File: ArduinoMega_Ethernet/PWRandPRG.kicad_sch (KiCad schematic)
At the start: 91 parts, among them J1 RJ45_Amphenol_RJMG1BD3B8K1ANR, J11 Micro_SD_Card_Det_Hirose_DM3AT, J9 PROGRAM_POWER_USBC, U2 CH340C, U3 ISM330DHCX, U4 W5500, U5 LM3281, U6 74HC244, U7 SE050C2HQ1, U8 AP22804AW5, U9 MCP7940N-xST, Y2 25Mhz, Y3 Crystal_GND23

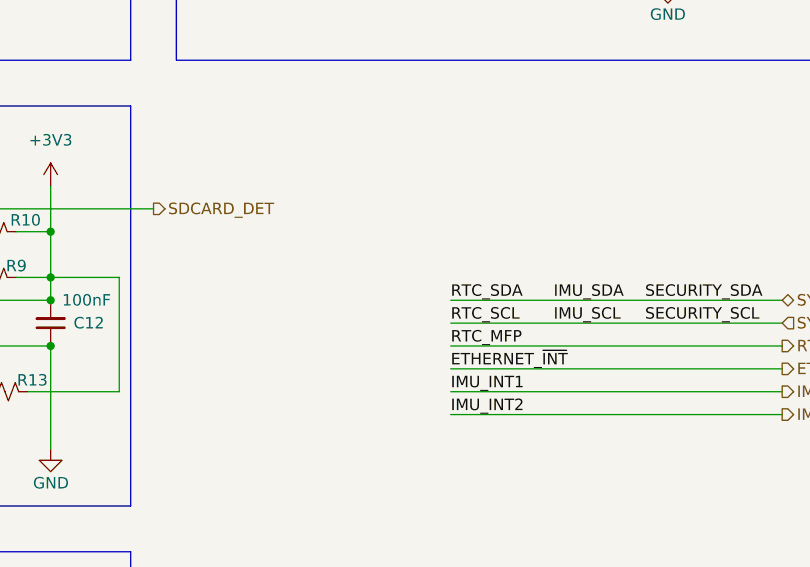
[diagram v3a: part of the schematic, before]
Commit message: I2C and Silkscreen revision
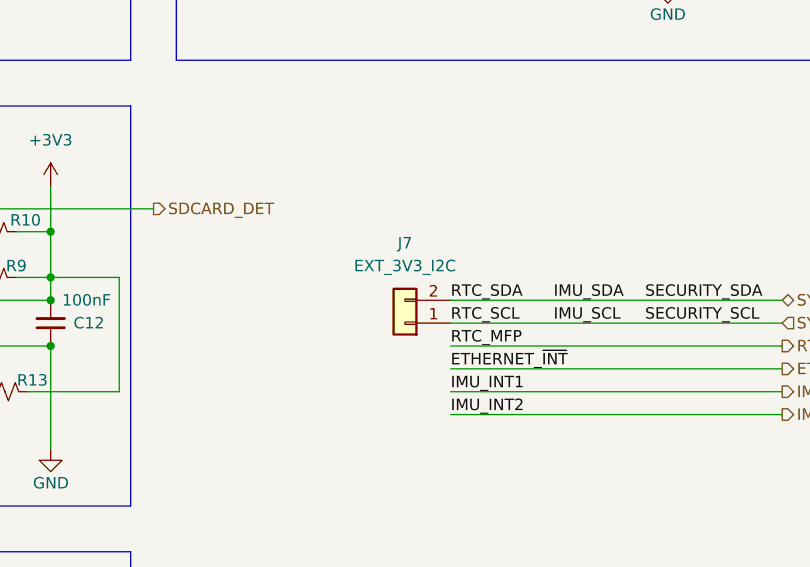
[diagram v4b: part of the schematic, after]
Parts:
- added J7: EXT_3V3_I2C, Connector_PinHeader_2.54mm:PinHeader_1x02_P2.54mm_Vertical, symbol Connector_Generic:Conn_01x02
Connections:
- net SYS_SCL: now also J7.1 (Pin_1)
- net SYS_SDA: now also J7.2 (Pin_2)
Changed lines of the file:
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@@
+	)
+	(symbol
+		(lib_id "Connector_Generic:Conn_01x02")
+		(at 240.03 208.28 180)
+		(unit 1)
+		(exclude_from_sim no)
+		(in_bom yes)
+		(on_board yes)
+		(dnp no)
+		(fields_autoplaced yes)
+		(property "Reference" "J7"
+			(at 240.03 199.39 0)
+			(effects
+				(font
+					(size 1.27 1.27)
+				)
+			)
+		)
+		(property "Value" "EXT_3V3_I2C"
+			(at 240.03 201.93 0)
+			(effects
+				(font
+					(size 1.27 1.27)
+				)
+			)
+		)
+		(property "Footprint" "Connector_PinHeader_2.54mm:PinHeader_1x02_P2.54mm_Vertical"
+			(at 240.03 208.28 0)
+			(effects
+				(font
+					(size 1.27 1.27)
+				)
+				(hide yes)
+			)
+		)
+		(property "Datasheet" "~"
+			(at 240.03 208.28 0)
+			(effects
+				(font
+					(size 1.27 1.27)
+				)
+				(hide yes)
+			)
+		)
+		(property "Description" "Generic connector, single row, 01x02, script generated (kicad-library-utils/schlib/autogen/connector/)"
+			(at 240.03 208.28 0)
+			(effects
+				(font
+					(size 1.27 1.27)
+				)
+				(hide yes)
+			)
+		)
+		(pin "1"
+		)
+		(pin "2"
+		)
+		(instances
+			(project ""
+				(path "/e63e39d7-6ac0-4ffd-8aa3-1841a4541b55/d82cdb2b-8484-4e54-a08e-6d3e852917b3"
+					(reference "J7")
+					(unit 1)
+				)
+			)
+		)
 	)
 	(symbol

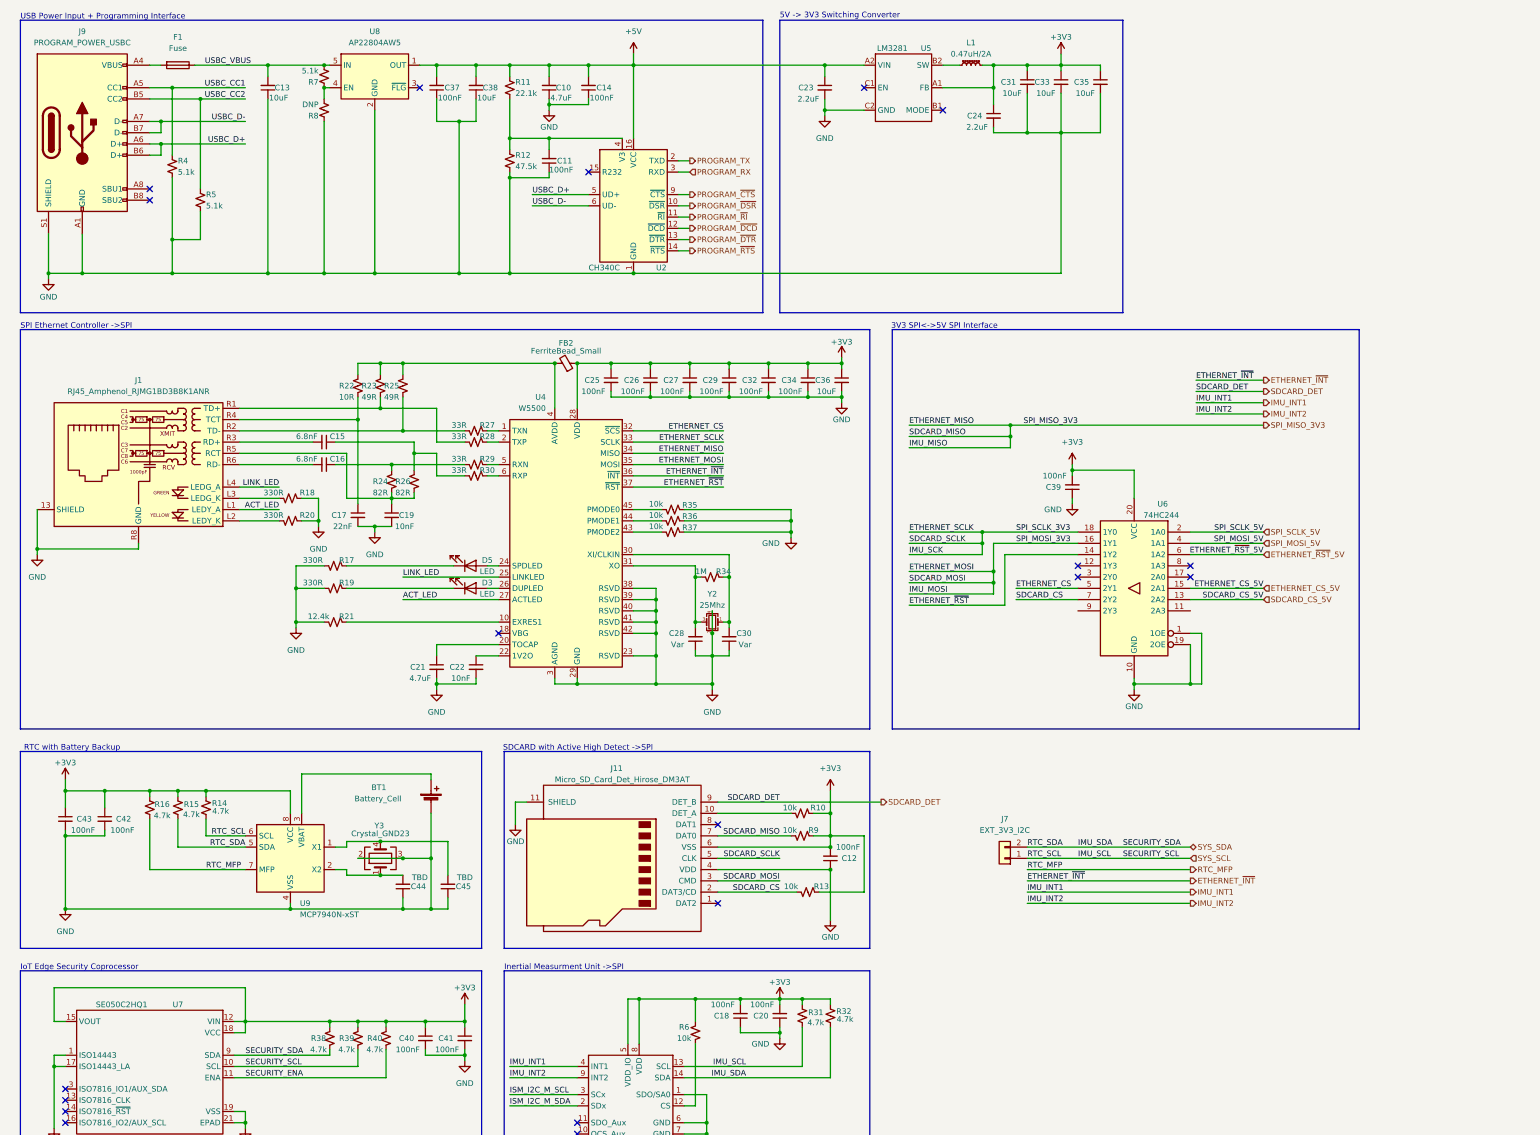
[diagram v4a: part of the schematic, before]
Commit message: update level shifter, configurable pmode
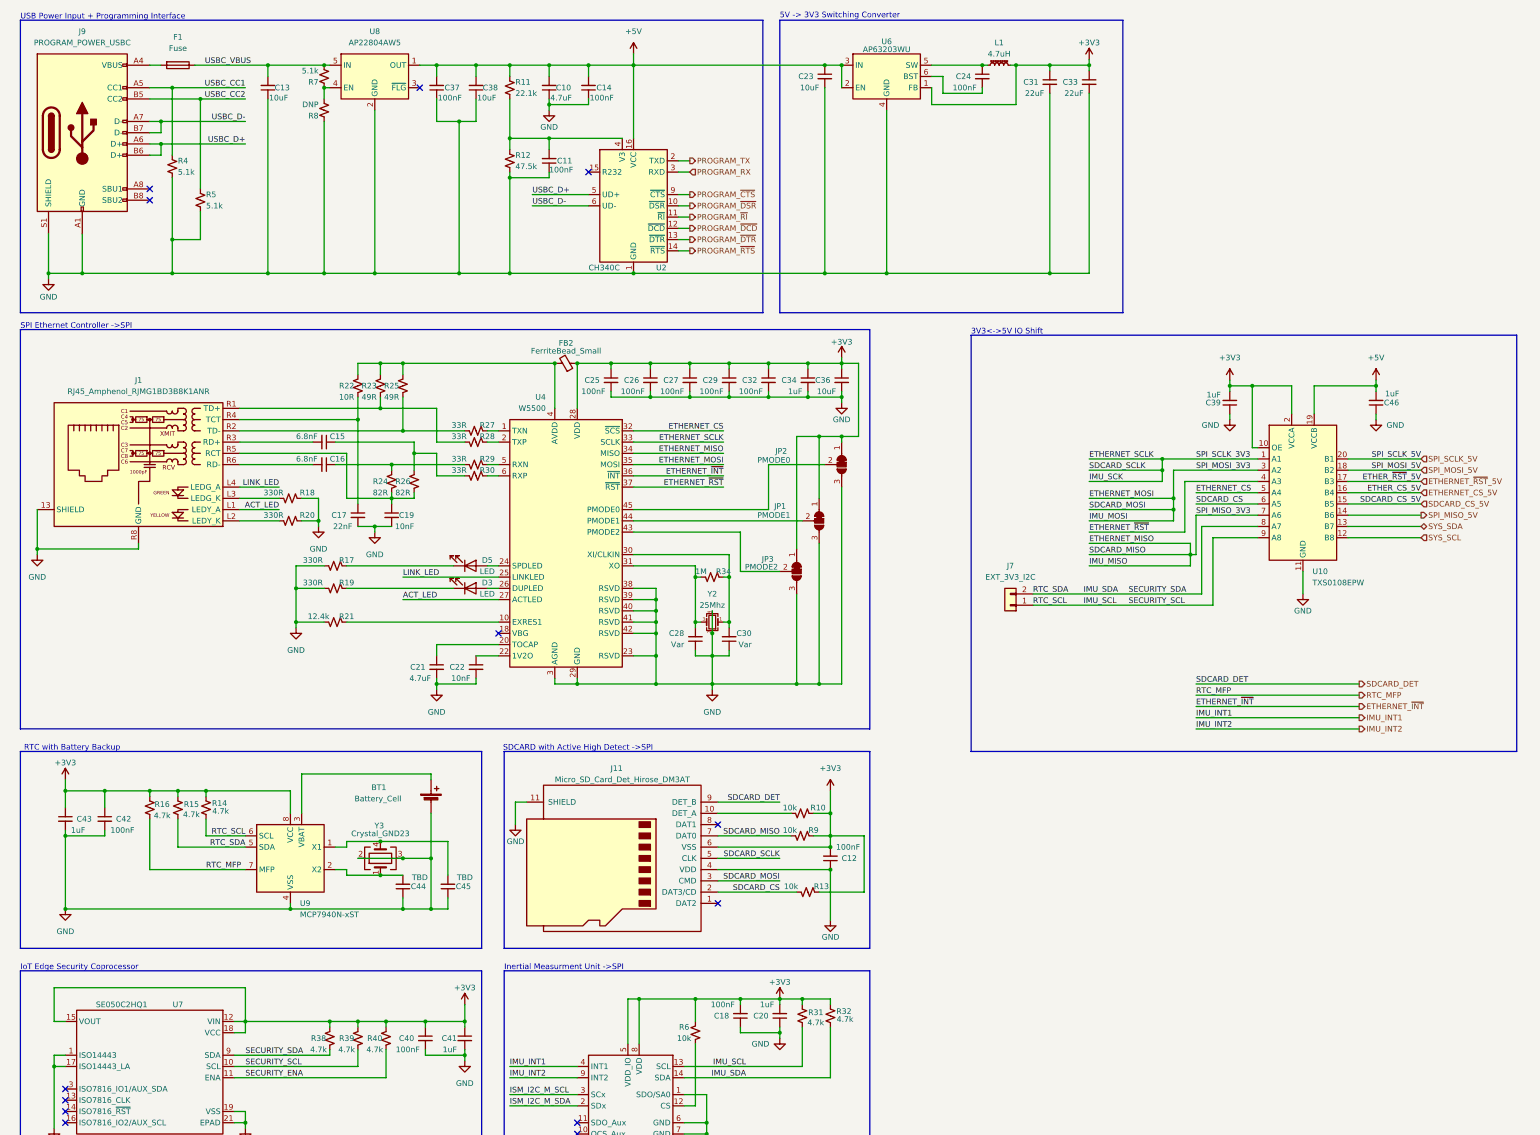
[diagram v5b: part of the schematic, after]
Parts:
- removed C35: 10uF, Capacitor_SMD:C_0805_2012Metric_Pad1.18x1.45mm_HandSolder, symbol Device:C_Small
- removed R35, R36, R37: 10k, Resistor_SMD:R_0603_1608Metric, symbol Device:R_Small_US
- removed U5: LM3281, Package_BGA:Texas_DSBGA-6_0.9x1.4mm_Layout2x3_P0.5mm, symbol DC_DC_Converters:LM3281
- removed U6: 74HC244, Package_DFN_QFN:WQFN-20-1EP_2.5x4.5mm_P0.5mm_EP1x2.9mm, symbol 74xx:74HC244
- added C46: 1uF, Capacitor_SMD:C_0603_1608Metric, symbol Device:C_Small
- added JP1: PMODE1, Jumper:SolderJumper-3_P1.3mm_Bridged12_Pad1.0x1.5mm, symbol Jumper:SolderJumper_3_Bridged12
- added JP2: PMODE0, Jumper:SolderJumper-3_P1.3mm_Bridged12_Pad1.0x1.5mm, symbol Jumper:SolderJumper_3_Bridged12
- added JP3: PMODE2, Jumper:SolderJumper-3_P1.3mm_Bridged12_Pad1.0x1.5mm, symbol Jumper:SolderJumper_3_Bridged12
- added U10: TXS0108EPW, Package_SO:TSSOP-20_4.4x6.5mm_P0.65mm, symbol Logic_LevelTranslator:TXS0108EPW
- added U6: AP63203WU, Package_TO_SOT_SMD:TSOT-23-6, symbol Regulator_Switching:AP63203WU
- C20, C34, C39, C41, C43: value 100nF -> 1uF
- C23: value 2.2uF -> 10uF
- C24: value 2.2uF -> 100nF
- C31, C33: value 10uF -> 22uF
- L1: value 0.47uH/2A -> 4.7uH; footprint Inductor_SMD:L_1206_3216Metric -> Inductor_SMD:L_1210_3225Metric_Pad1.42x2.65mm_HandSolder
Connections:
- net +3V3: now also JP1.1 (A), JP2.1 (A), JP3.1 (A), U10.10 (OE), U10.2 (VCCA), U6.1 (FB); no longer C24.1
- net +5V: now also C46.2, U10.19 (VCCB), U6.2 (EN), U6.3 (IN)
- net ETHERNET_CS: now also U10.5 (A4)
- net ETHERNET_CS_5V: now also U10.16 (B4)
- net ETHERNET_MOSI: now also U10.3 (A2)
- net ETHERNET_SCLK: now also U10.1 (A1)
- net ETHERNET_~{RST}: now also U10.4 (A3)
- net ETHERNET_~{RST}_5V: now also U10.17 (B3)
- net GND: now also C46.1, JP1.3 (B), JP2.3 (B), JP3.3 (B), U10.11 (GND), U6.4 (GND); no longer C24.2
- net SDCARD_CS: now also U10.6 (A5)
- net SDCARD_CS_5V: now also U10.15 (B5)
- net SPI_MOSI_5V: now also U10.18 (B2)
- net SPI_SCLK_5V: now also U10.20 (B1)
- net SYS_SCL: now also U10.12 (B8); no longer J7.1 (Pin_1), R14.2, R31.2, R39.2, U3.13 (SCL), U7.10 (SCL), U9.6 (SCL)
- net SYS_SDA: now also U10.13 (B7); no longer J7.2 (Pin_2), R15.2, R32.2, R38.2, U3.14 (SDA), U7.9 (SDA), U9.5 (SDA)
- net at U4.45 (PMODE0): now also JP2.2 (C)
- net at U4.44 (PMODE1): now also JP1.2 (C)
- net at L1.1: now also C24.1, U6.5 (SW)
- net at U4.43 (PMODE2): now also JP3.2 (C)
- net SPI_MISO_3V3 renamed ETHERNET_MISO
- net ETHERNET_MISO: now also U10.7 (A6)
- new net: C24.2, U6.6 (BST)
- new net IMU_SCL: J7.1 (Pin_1), R14.2, R31.2, R39.2, U10.9 (A8), U3.13 (SCL), U7.10 (SCL), U9.6 (SCL)
- new net IMU_SDA: J7.2 (Pin_2), R15.2, R32.2, R38.2, U10.8 (A7), U3.14 (SDA), U7.9 (SDA), U9.5 (SDA)
- new net SPI_MISO_5V: U10.14 (B6)
- no-connect marks 19 -> 13
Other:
- note added: "3V3<->5V IO Shift"
- note removed: "3V3 SPI<->5V SPI Interface"
- moved on the sheet: C23, C24, C31, C33, C39, J7, L1

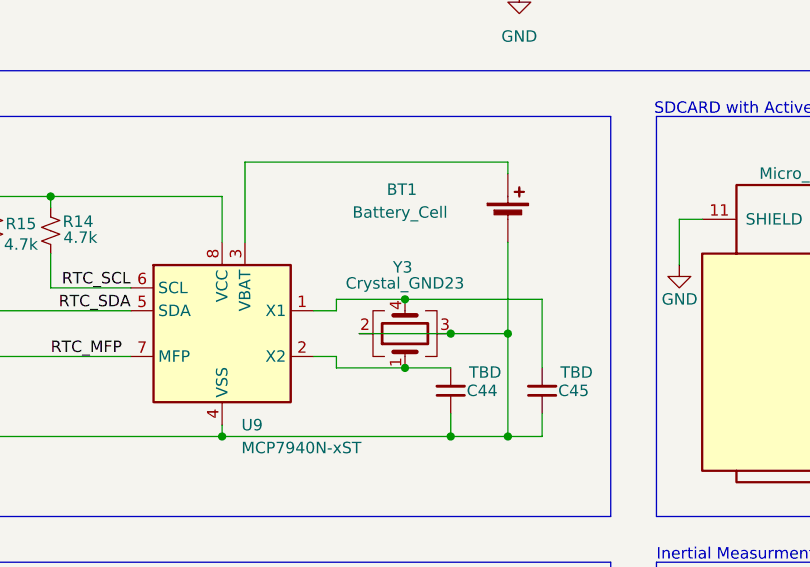
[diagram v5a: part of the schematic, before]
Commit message: Add files via upload
fix undersized capacitors
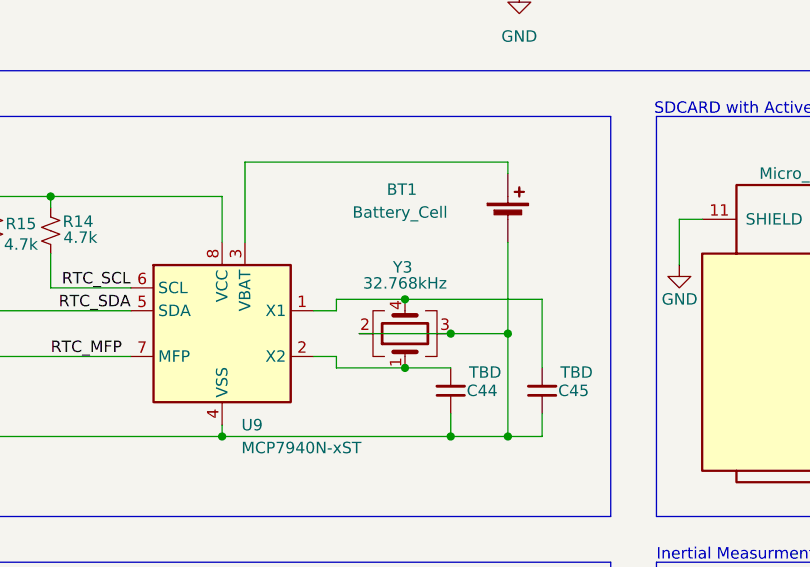
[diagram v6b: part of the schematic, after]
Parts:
- C10, C21, C23: footprint Capacitor_SMD:C_0603_1608Metric -> Capacitor_SMD:C_0805_2012Metric_Pad1.18x1.45mm_HandSolder
- C31, C33: footprint Capacitor_SMD:C_0805_2012Metric_Pad1.18x1.45mm_HandSolder -> Capacitor_SMD:C_1210_3225Metric_Pad1.33x2.70mm_HandSolder
- Y3: value Crystal_GND23 -> 32.768kHz
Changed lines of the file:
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@@
 			)
 		)
-		(property "Footprint" "Capacitor_SMD:C_0603_1608Metric"
+		(property "Footprint" "Capacitor_SMD:C_0805_2012Metric_Pad1.18x1.45mm_HandSolder"
 			(at 137.16 34.29 0)
 			(effects
@@
 			)
 		)
-		(property "Value" "Crystal_GND23"
+		(property "Value" "32.768kHz"
 			(at 99.06 202.692 90)
 			(effects
@@
 			)
 		)
-		(property "Footprint" "Capacitor_SMD:C_0805_2012Metric_Pad1.18x1.45mm_HandSolder"
+		(property "Footprint" "Capacitor_SMD:C_1210_3225Metric_Pad1.33x2.70mm_HandSolder"
 			(at 259.08 33.02 0)
 			(effects
@@
 			)
 		)
-		(property "Footprint" "Capacitor_SMD:C_0603_1608Metric"
+		(property "Footprint" "Capacitor_SMD:C_0805_2012Metric_Pad1.18x1.45mm_HandSolder"
 			(at 199.39 31.75 0)
 			(effects
@@
 			)
 		)
-		(property "Footprint" "Capacitor_SMD:C_0805_2012Metric_Pad1.18x1.45mm_HandSolder"
+		(property "Footprint" "Capacitor_SMD:C_1210_3225Metric_Pad1.33x2.70mm_HandSolder"
 			(at 250.19 33.02 0)
 			(effects
@@
 			)
 		)
-		(property "Footprint" "Capacitor_SMD:C_0603_1608Metric"
+		(property "Footprint" "Capacitor_SMD:C_0805_2012Metric_Pad1.18x1.45mm_HandSolder"
 			(at 111.76 165.1 0)
 			(effects

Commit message: fix VIN pin
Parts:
- added C35: 10uF, Capacitor_SMD:C_0805_2012Metric_Pad1.18x1.45mm_HandSolder, symbol Device:C_Small
- added C47: 100nF, Capacitor_SMD:C_0603_1608Metric, symbol Device:C_Small
- added C48, C49: 22uF, Capacitor_SMD:C_1210_3225Metric_Pad1.33x2.70mm_HandSolder, symbol Device:C_Small
- added L2: 4.7uH, Inductor_SMD:L_1210_3225Metric_Pad1.42x2.65mm_HandSolder, symbol Device:L_Ferrite_Small
- added U5: AP63205WU, Package_TO_SOT_SMD:TSOT-23-6, symbol Regulator_Switching:AP63203WU
- L1: value 4.7uH -> 3.9uH
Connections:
- net +5V: now also C48.1, C49.1, L2.2, U5.1 (FB)
- net GND: now also C35.2, C48.2, C49.2, U5.4 (GND)
- new net: C47.1, L2.1, U5.5 (SW)
- new net: C47.2, U5.6 (BST)
- new net VIN+: C35.1, U5.2 (EN), U5.3 (IN)
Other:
- note added: "VIN Pin (5.5V - 32V) -> 5V0 Switching Converter"
- moved on the sheet: BT1, C12, C15, C16, C17, C18, C19, C20, C21, C22, C25, C26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

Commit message: finished BOM and component sizing
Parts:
- C28, C30: value Var -> 18pF; footprint Capacitor_SMD:C_0603_1608Metric -> Capacitor_SMD:C_0402_1005Metric_Pad0.74x0.62mm_HandSolder
- C44, C45: value TBD -> 12pF; footprint Capacitor_SMD:C_0603_1608Metric -> Capacitor_SMD:C_0402_1005Metric_Pad0.74x0.62mm_HandSolder
- L1, L2: footprint Inductor_SMD:L_1210_3225Metric_Pad1.42x2.65mm_HandSolder -> Inductor_SMD:L_APV_ANR6028
- Y3: footprint Crystal:Crystal_SMD_3225-4Pin_3.2x2.5mm_HandSoldering -> Crystal:Crystal_SMD_EuroQuartz_EQ161-2Pin_3.2x1.5mm_HandSoldering; symbol Device:Crystal_GND23 -> Device:Crystal
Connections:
- net GND: no longer Y3.2, Y3.3
- net at C45.2, U9.1 (X1): now also Y3.2; no longer Y3.4
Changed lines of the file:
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@@
 	)
 	(junction
-		(at 102.87 260.35)
-		(diameter 0)
-		(color 0 0 0 0)
-	)
-	(junction
 		(at 59.69 194.31)
 		(diameter 0)
@@
 	)
 	(junction
-		(at 109.22 260.35)
-		(diameter 0)
-		(color 0 0 0 0)
-	)
-	(junction
 		(at 168.91 160.02)
 		(diameter 0)
@@
 	(wire
 		(pts
-			(xy 102.87 260.35) (xy 109.22 260.35)
-		)
-		(stroke
-			(width 0)
-			(type default)
-		)
-	)
-	(wire
-		(pts
 			(xy 321.31 132.08) (xy 340.36 132.08)
 		)
@@
 	(wire
 		(pts
-			(xy 92.71 260.35) (xy 102.87 260.35)
-		)
-		(stroke
-			(width 0)
-			(type default)
-		)
-	)
-	(wire
-		(pts
 			(xy 168.91 167.64) (xy 172.72 167.64)
 		)
@@
 	(wire
 		(pts
-			(xy 109.22 250.19) (xy 109.22 260.35)
+			(xy 109.22 250.19) (xy 109.22 271.78)
 		)
 		(stroke
@@
 	(wire
 		(pts
-			(xy 109.22 260.35) (xy 109.22 271.78)
-		)
-		(stroke
-			(width 0)
-			(type default)
-		)
-	)
-	(wire
-		(pts
 			(xy 344.17 142.24) (xy 344.17 139.7)
 		)
@@
 			)
 		)
-		(property "Value" "Var"
-			(at 181.61 165.1 0)
+		(property "Value" "18pF"
+			(at 183.134 165.354 0)
 			(effects
 				(font
@@
 			)
 		)
-		(property "Footprint" "Capacitor_SMD:C_0603_1608Metric"
+		(property "Footprint" "Capacitor_SMD:C_0402_1005Metric_Pad0.74x0.62mm_HandSolder"
 			(at 176.53 163.83 0)
 			(effects
@@
 			)
 		)
-		(property "Value" "TBD"
-			(at 104.902 264.668 0)
+		(property "Value" "12pF"
+			(at 104.14 264.668 0)
 			(effects
 				(font
@@
 			)
 		)
-		(property "Footprint" "Capacitor_SMD:C_0603_1608Metric"
+		(property "Footprint" "Capacitor_SMD:C_0402_1005Metric_Pad0.74x0.62mm_HandSolder"
 			(at 102.87 266.7 0)
 			(effects
@@
 			)
 		)
-		(property "Value" "TBD"
-			(at 115.062 264.668 0)
+		(property "Value" "12pF"
+			(at 113.792 264.668 0)
 			(effects
 				(font
@@
 			)
 		)
-		(property "Footprint" "Capacitor_SMD:C_0603_1608Metric"
+		(property "Footprint" "Capacitor_SMD:C_0402_1005Metric_Pad0.74x0.62mm_HandSolder"
 			(at 113.03 266.7 0)
 			(effects
@@
 	)
 	(symbol
-		(lib_id "Device:Crystal_GND23")
+		(lib_id "Device:Crystal")
 		(at 97.79 260.35 90)
 		(unit 1)
@@
 			)
 		)
-		(property "Footprint" "Crystal:Crystal_SMD_3225-4Pin_3.2x2.5mm_HandSoldering"
+		(property "Footprint" "Crystal:Crystal_SMD_EuroQuartz_EQ161-2Pin_3.2x1.5mm_HandSoldering"
 			(at 97.79 260.35 0)
 			(effects
@@
 			)
 		)
-		(property "Description" "Four pin crystal, GND on pins 2 and 3"
+		(property "Description" "Two pin crystal"
 			(at 97.79 260.35 0)
 			(effects
@@
 			)
 		)
-		(pin "4"
-		)
 		(pin "1"
 		)
 		(pin "2"
 		)
-		(pin "3"
-		)
 		(instances
 			(project ""
@@
 		(on_board yes)
 		(dnp no)
-		(fields_autoplaced yes)
 		(property "Reference" "C28"
 			(at 166.37 162.5535 0)
@@
 			)
 		)
-		(property "Value" "Var"
-			(at 166.37 165.0935 0)
+		(property "Value" "18pF"
+			(at 164.084 165.1 0)
 			(effects
 				(font
 					(size 1.27 1.27)
 				)
-				(justify right)
+				(justify top)
 			)
 		)
-		(property "Footprint" "Capacitor_SMD:C_0603_1608Metric"
+		(property "Footprint" "Capacitor_SMD:C_0402_1005Metric_Pad0.74x0.62mm_HandSolder"
 			(at 168.91 163.83 0)
 			(effects
@@
 					(size 1.27 1.27)
 				)
+				(justify top)
 				(hide yes)
 			)
@@
 			)
 		)
-		(property "Footprint" "Inductor_SMD:L_1210_3225Metric_Pad1.42x2.65mm_HandSolder"
+		(property "Footprint" "Inductor_SMD:L_APV_ANR6028"
 			(at 238.76 29.21 0)
 			(effects
@@
 			)
 		)
-		(property "Footprint" "Inductor_SMD:L_1210_3225Metric_Pad1.42x2.65mm_HandSolder"
+		(property "Footprint" "Inductor_SMD:L_APV_ANR6028"
 			(at 318.77 30.48 0)
 			(effects
